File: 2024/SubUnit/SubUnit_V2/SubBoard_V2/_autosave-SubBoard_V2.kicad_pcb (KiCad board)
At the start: 2 copper layers, 66.8 x 58 mm, 30 parts, among them J1 Conn_01x02_Socket, J10 Conn_01x02_Socket, J11 Conn_01x03_Socket, J12 Conn_01x02_Socket, J13 Conn_01x02_Socket, J14 Conn_01x05_Socket, J15 Conn_01x05_Socket, J16 Conn_01x02_Socket, J18 Conn_01x07_Socket, J19 Conn_01x07_Socket, J2 Conn_01x02_Socket, J3 Conn_01x02_Socket, J4 Conn_01x02_Socket, J5 Conn_01x02_Socket, J6 Conn_01x02_Socket, J7 Conn_01x02_Socket, J8 Conn_01x02_Socket, J9 Conn_01x02_Socket

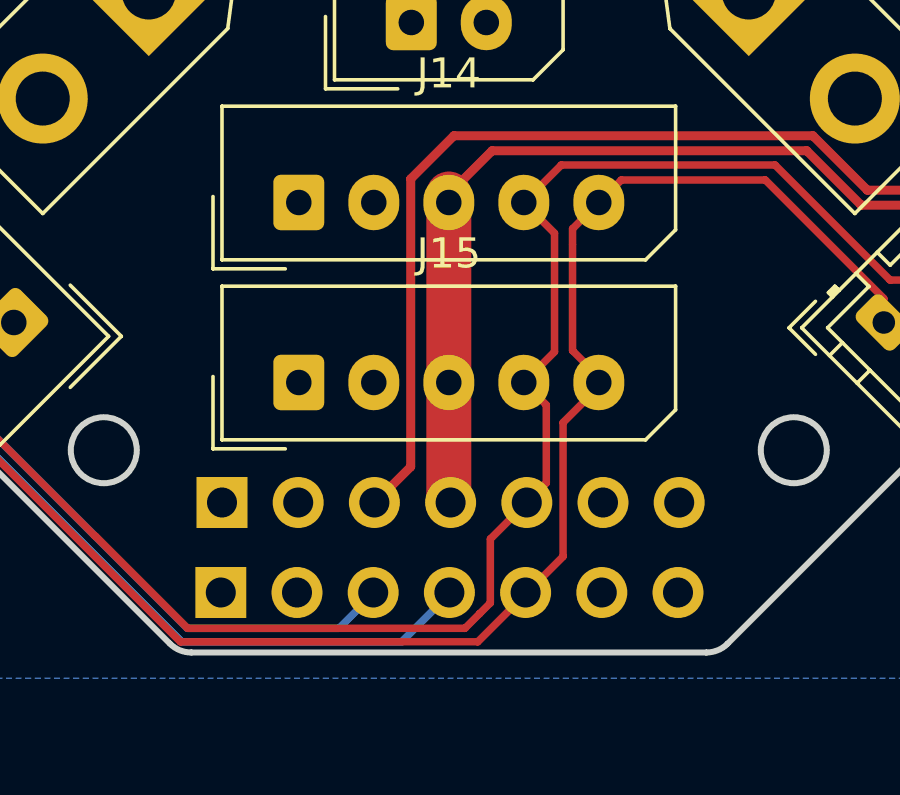
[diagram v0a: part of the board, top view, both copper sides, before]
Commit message: ✏️CANBUSの距離を近づけたり、角度変化を少し緩やかにした
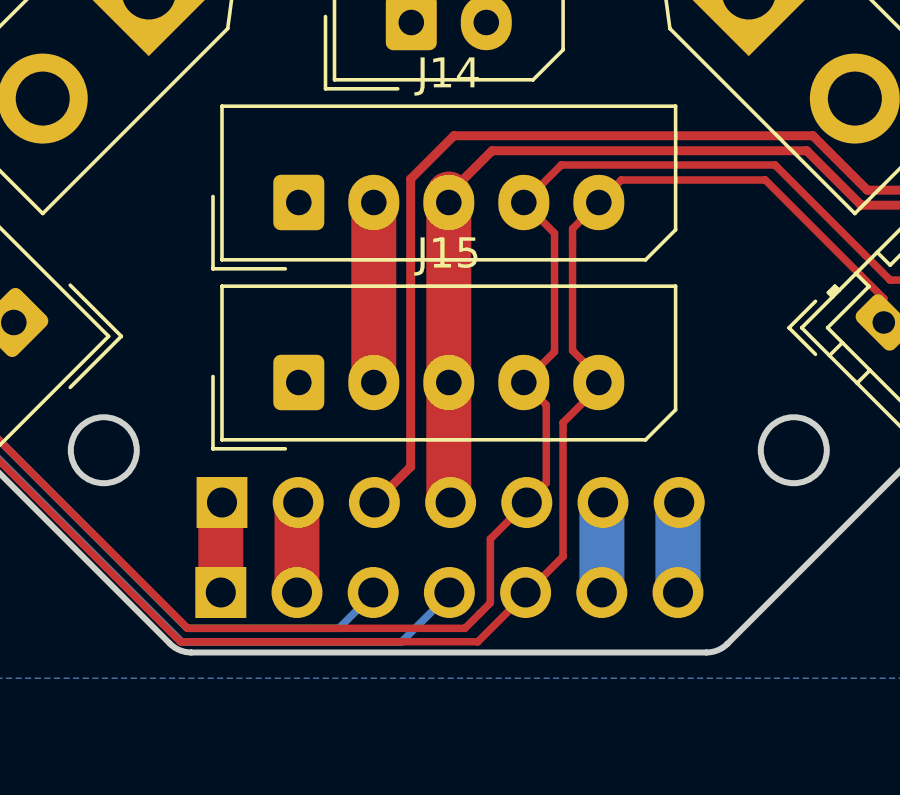
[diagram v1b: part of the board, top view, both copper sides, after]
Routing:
- net +15V: track 0.00 -> 12.0 mm
- net GNDPWR: track 15.2 -> 21.3 mm
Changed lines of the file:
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@@
     (effects (font (size 0.8 0.8) (thickness 0.1) italic) (justify left bottom mirror))
   )
+  (segment (start -2.5 14) (end -2.5 20) (width 1.5) (layer "F.Cu") (net 1))
+  (segment (start -7.6 27) (end -7.6 24.04) (width 1.5) (layer "F.Cu") (net 1))
+  (segment (start -5.06 24.04) (end -5.02 24) (width 1.5) (layer "F.Cu") (net 1))
+  (segment (start -7.6 24.04) (end -7.56 24) (width 1.5) (layer "F.Cu") (net 1))
+  (segment (start -5.06 27) (end -5.06 24.04) (width 1.5) (layer "F.Cu") (net 1))
   (segment (start -19.05 18.542) (end -19.05 15.147056) (width 0.25) (layer "F.Cu") (net 2))
   (segment (start -19.05 15.147056) (end -22 12.197056) (width 0.25) (layer "F.Cu") (net 2))
@@
   (segment (start 17.272 -17.526) (end 17.272 -17.729) (width 0.3) (layer "F.Cu") (net 7))
   (segment (start 19.2035 -15.5945) (end 19.2035 -10.16) (width 0.3) (layer "F.Cu") (net 7))
+  (segment (start 7.64 24.04) (end 7.68 24) (width 1.5) (layer "B.Cu") (net 7))
+  (segment (start 7.64 27) (end 7.64 24.04) (width 1.5) (layer "B.Cu") (net 7))
+  (segment (start 5.1 24.04) (end 5.14 24) (width 1.5) (layer "B.Cu") (net 7))
+  (segment (start 5.1 27) (end 5.1 24.04) (width 1.5) (layer "B.Cu") (net 7))
   (segment (start 22.098 -20.32) (end 22.098 -8.636) (width 0.3) (layer "F.Cu") (net 8))
   (segment (start 13.744752 14.089) (end 11.930752 12.275) (width 0.3) (layer "F.Cu") (net 8))
@@
       )
     )
+  )
+  (zone (net 0) (net_name "") (layer "B.Cu") (hatch edge 0.5)
+    (connect_pads (clearance 0))
+    (min_thickness 0.25) (filled_areas_thickness no)
+    (keepout (tracks allowed) (vias allowed) (pads allowed) (copperpour not_allowed) (footprints allowed))
+    (fill (thermal_gap 0.5) (thermal_bridge_width 0.5))
+    (polygon
+      (pts
+        (xy -3.556 22.352)
+        (xy -9.144 22.352)
+        (xy -9.144 26.924)
+        (xy -3.556 26.924)
+      )
+    )
